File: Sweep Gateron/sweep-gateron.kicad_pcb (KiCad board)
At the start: 2 copper layers, 229.5 x 95.2 mm, 61 parts, among them J1 AudioJack4dpb, J2 AudioJack4dpb, SW10 SW_Push, SW10_r1 SW_Push, SW11 SW_Push, SW11_r1 SW_Push, SW12 SW_Push, SW12_r1 SW_Push, SW13_r1 SW_Push, SW14 SW_Push, SW14_r1 SW_Push, SW15 SW_Push, SW15_r1 SW_Push, SW16 SW_Push, SW16_r1 SW_Push, SW17 SW_Push, SW18 SW_Push, SW2 SW_Push, SW2 SW_SPDT, SW20 SW_Push, SW21 SW_Push, SW2_r1 SW_Push, SW3 SW_Push, SW3_r1 SW_Push, SW4 SW_Push, SW4_r1 SW_Push, SW5 SW_Push, SW5_r1 SW_Push, SW6 SW_Push, SW6_r1 SW_Push, SW7_r1 SW_Push, SW8 SW_Push, SW8_r1 SW_Push, SW9 SW_Push, SW9_r1 SW_Push, U1 ProMicro-kbd, U2 ProMicro-kbd

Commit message: Had my friend look at the board, routing seems okay. Added some via stitches for better ground plane continuity
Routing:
- net gnd: track 2.89 -> 0.00 mm, vias 1 -> 33

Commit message: Added gerber files
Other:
- board text added: "There is no prize to perfection, only an end to pursuit"
- board text removed: "The Aeroplane Flies High (Turns Left, Looks Right)"
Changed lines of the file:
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@@
 		)
 		(fp_text user "RESET"
-			(at 0 2.286 90)
-			(layer "B.SilkS")
+			(at 0 -4.2 90)
+			(layer "F.SilkS")
 			(effects
 				(font
@@
 		(fp_text user "RESET"
 			(at 0 2.286 90)
-			(layer "B.SilkS")
+			(layer "F.SilkS")
 			(effects
 				(font
@@
 	(gr_text "Face down"
 		(at 160.10984 99.23 90)
-		(layer "F.SilkS")
+		(layer "B.SilkS")
 		(effects
 			(font
@@
 		)
 	)
-	(gr_text "Face down"
-		(at 139.7 99.06 90)
-		(layer "F.SilkS")
+	(gr_text "There is no prize to perfection, only an end to pursuit"
+		(at 232.5 123 0)
+		(layer "B.SilkS")
 		(effects
 			(font
@@
 				(thickness 0.3)
 			)
+			(justify mirror)
 		)
 	)
-	(gr_text "The Aeroplane Flies High (Turns Left, Looks Right)"
-		(at 233.62984 122.936 0)
+	(gr_text "Face down"
+		(at 139.7 99.06 90)
 		(layer "B.SilkS")
 		(effects
@@
 				(thickness 0.3)
 			)
-			(justify mirror)
 		)
 	)

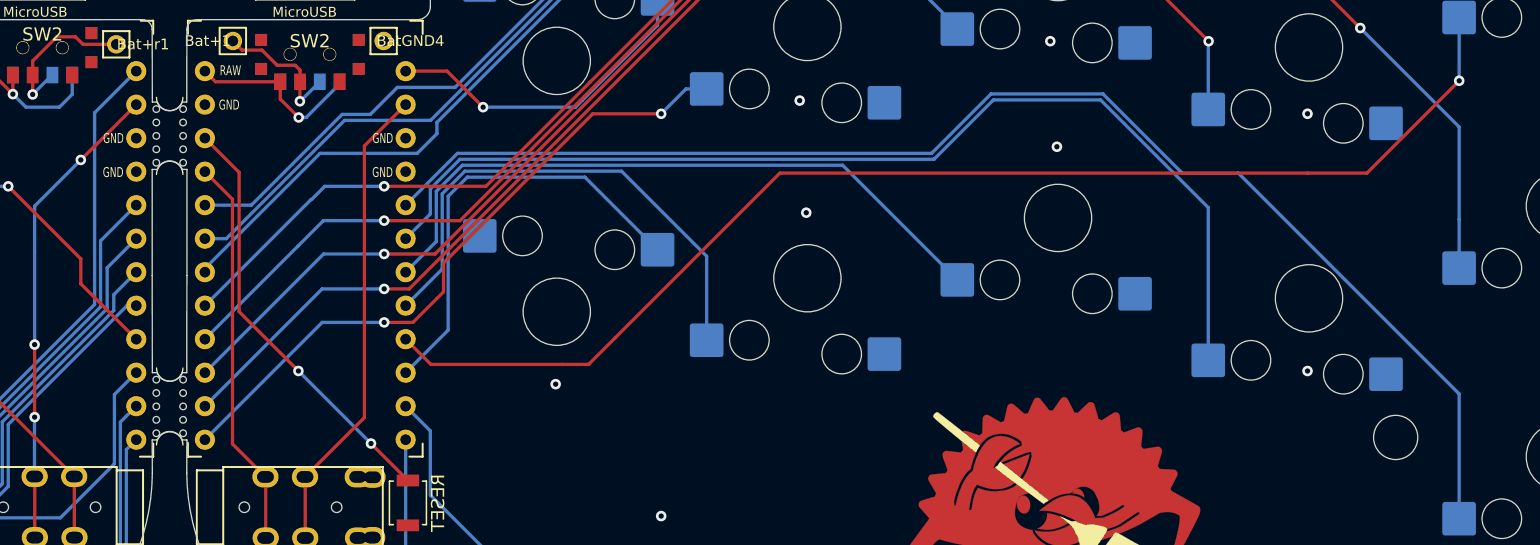
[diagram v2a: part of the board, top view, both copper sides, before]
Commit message: Fixed swapped pads and generated gerber files
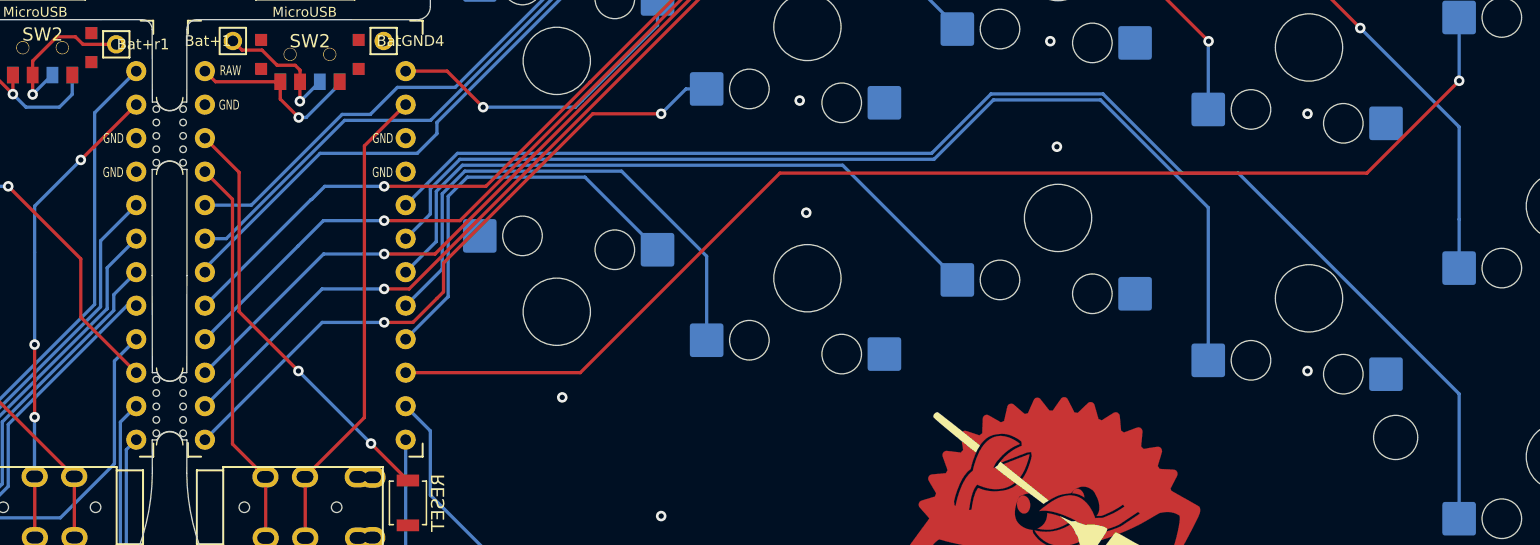
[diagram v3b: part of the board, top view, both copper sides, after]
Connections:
- U1 pad 10: Switch15 -> Switch1
- U1 pad 9: Switch1 -> Switch15
- U2 pad 10: Switch15_r -> Switch1_r
- U2 pad 9: Switch1_r -> Switch15_r
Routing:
- net Switch15_r: track 33.5 -> 30.9 mm
- net Switch15: track 46.5 -> 49.1 mm
- net Switch1: track 129.2 -> 131.8 mm
- net Switch1_r: track 94.4 -> 93.8 mm
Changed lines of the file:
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@@
 			(layers "*.Cu" "B.Mask" "F.SilkS")
 			(remove_unused_layers no)
-			(net 6 "Switch1")
+			(net 20 "Switch15")
 			(pinfunction "D7")
 			(pintype "bidirectional")
@@
 			(layers "*.Cu" "B.Mask" "F.SilkS")
 			(remove_unused_layers no)
-			(net 20 "Switch15")
+			(net 6 "Switch1")
 			(pinfunction "E6")
 			(pintype "bidirectional")
@@
 			(layers "*.Cu" "B.Mask" "F.SilkS")
 			(remove_unused_layers no)
-			(net 36 "Switch1_r")
+			(net 33 "Switch15_r")
 			(pinfunction "D7")
 			(pintype "bidirectional")
@@
 			(layers "*.Cu" "B.Mask" "F.SilkS")
 			(remove_unused_layers no)
-			(net 33 "Switch15_r")
+			(net 36 "Switch1_r")
 			(pinfunction "E6")
 			(pintype "bidirectional")
@@
 	)
 	(via
-		(at 179.5 109.5)
+		(at 180 110.5)
 		(size 0.8)
 		(drill 0.4)
@@
 	)
 	(segment
-		(start 138 94.5)
-		(end 143.5 100)
+		(start 143.5 104.4226)
+		(end 147.7054 108.628)
 		(width 0.25)
 		(layer "F.Cu")
@@
 	)
 	(segment
-		(start 143.5 101.8826)
-		(end 147.7054 106.088)
+		(start 143.5 100)
+		(end 143.5 104.4226)
 		(width 0.25)
 		(layer "F.Cu")
@@
 	)
 	(segment
-		(start 143.5 100)
-		(end 143.5 101.8826)
+		(start 138 94.5)
+		(end 143.5 100)
 		(width 0.25)
 		(layer "F.Cu")
@@
 	)
 	(segment
-		(start 119.58657 111)
-		(end 125.84157 117.255)
+		(start 141.955816 119.632084)
+		(end 146.049 115.5389)
 		(width 0.25)
 		(layer "B.Cu")
@@
 	)
 	(segment
-		(start 141.955816 119.632084)
-		(end 146.049 115.5389)
+		(start 146.049 107.7444)
+		(end 147.7054 106.088)
 		(width 0.25)
 		(layer "B.Cu")
@@
 	)
 	(segment
-		(start 146.049 110.2844)
-		(end 147.7054 108.628)
+		(start 125.84157 117.255)
+		(end 131.005 117.255)
 		(width 0.25)
 		(layer "B.Cu")
@@
 	(segment
 		(start 146.049 115.5389)
-		(end 146.049 110.2844)
+		(end 146.049 107.7444)
 		(width 0.25)
 		(layer "B.Cu")
@@
 	)
 	(segment
-		(start 131.005 117.255)
-		(end 133.382084 119.632084)
+		(start 133.382084 119.632084)
+		(end 141.955816 119.632084)
 		(width 0.25)
 		(layer "B.Cu")
@@
 	)
 	(segment
-		(start 125.84157 117.255)
-		(end 131.005 117.255)
+		(start 115.6345 111)
+		(end 119.58657 111)
 		(width 0.25)
 		(layer "B.Cu")
@@
 	)
 	(segment
-		(start 115.6345 111)
-		(end 119.58657 111)
+		(start 131.005 117.255)
+		(end 133.382084 119.632084)
 		(width 0.25)
 		(layer "B.Cu")
@@
 	)
 	(segment
-		(start 133.382084 119.632084)
-		(end 141.955816 119.632084)
+		(start 119.58657 111)
+		(end 125.84157 117.255)
 		(width 0.25)
 		(layer "B.Cu")
@@
 	)
 	(segment
-		(start 168.12924 108.628)
-		(end 171.353 105.40424)
+		(start 181.71934 93.804)
+		(end 187.22334 99.308)
 		(width 0.25)
 		(layer "B.Cu")
@@
 	)
 	(segment
-		(start 181.71934 93.804)
-		(end 187.22334 99.308)
+		(start 172.80448 93.804)
+		(end 181.71934 93.804)
 		(width 0.25)
 		(layer "B.Cu")
@@
 	)
 	(segment
-		(start 172.80448 93.804)
-		(end 181.71934 93.804)
+		(start 171.353 95.25548)
+		(end 172.80448 93.804)
 		(width 0.25)
 		(layer "B.Cu")
@@
 	)
 	(segment
-		(start 171.353 105.40424)
-		(end 171.353 95.25548)
+		(start 171.353 102.86424)
+		(end 168.12924 106.088)
 		(width 0.25)
 		(layer "B.Cu")
@@
 	(segment
 		(start 171.353 95.25548)
-		(end 172.80448 93.804)
+		(end 171.353 102.86424)
 		(width 0.25)
 		(layer "B.Cu")
@@
 	)
 	(segment
-		(start 182 108)
-		(end 184 106)
-		(width 0.25)
-		(layer "F.Cu")
-		(net 36)
-	)
-	(segment
-		(start 180 108)
-		(end 182 108)
+		(start 196.5 93.5)
+		(end 181.372 108.628)
 		(width 0.25)
 		(layer "F.Cu")
@@
 	)
 	(segment
-		(start 168.12924 106.088)
-		(end 170.04124 108)
+		(start 181.372 108.628)
+		(end 168.12924 108.628)
 		(width 0.25)
 		(layer "F.Cu")
@@
 	(segment
 		(start 241 93.5)
-		(end 248 86.5)
-		(width 0.25)
-		(layer "F.Cu")
-		(net 36)
-	)
-	(segment
-		(start 236.5 93.5)
-		(end 241 93.5)
-		(width 0.25)
-		(layer "F.Cu")
-		(net 36)
-	)
-	(segment
-		(start 196.5 93.5)
-		(end 236.5 93.5)
-		(width 0.25)
-		(layer "F.Cu")
-		(net 36)
-	)
-	(segment
-		(start 184 106)
 		(end 196.5 93.5)
 		(width 0.25)
@@
 	)
 	(segment
-		(start 170.04124 108)
-		(end 180 108)
+		(start 248 86.5)
+		(end 241 93.5)
 		(width 0.25)
 		(layer "F.Cu")
